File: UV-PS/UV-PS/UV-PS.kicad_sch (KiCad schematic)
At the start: 15 parts, among them J1 Conn_01x02_Female, J2 Conn_01x02_Female, U1 MC33063AP

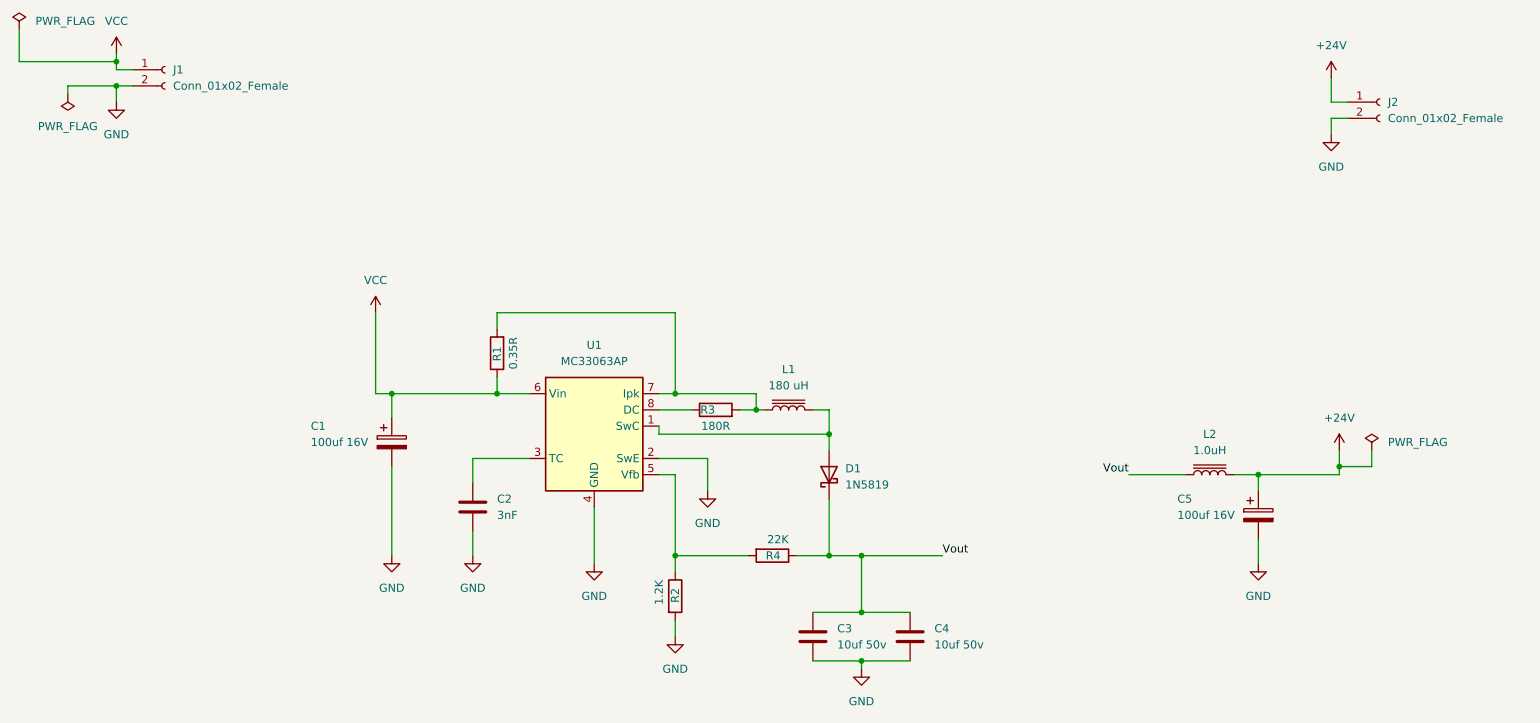
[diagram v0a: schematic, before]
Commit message: IC Change
Changed complete design.
From Mc33062 to LMR64010
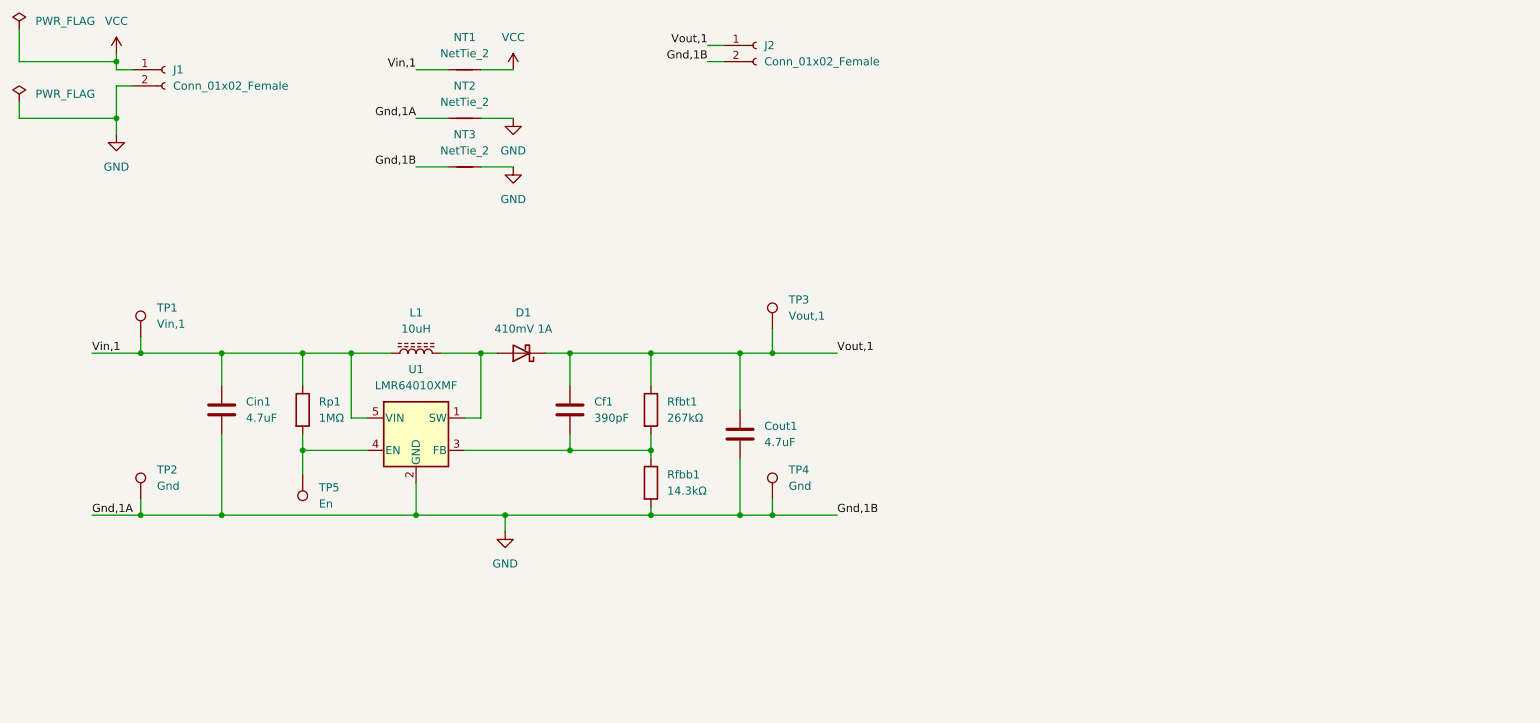
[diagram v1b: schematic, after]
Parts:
- removed C1, C5: 100uf 16V, Capacitor_THT:CP_Radial_D6.3mm_P2.50mm, symbol Device:C_Polarized
- removed C2: 3nF, Capacitor_SMD:C_0603_1608Metric_Pad1.08x0.95mm_HandSolder, symbol Device:C
- removed C3, C4: 10uf 50v, Capacitor_SMD:C_1206_3216Metric_Pad1.33x1.80mm_HandSolder, symbol Device:C
- removed D1: 1N5819, Diode_THT:D_DO-41_SOD81_P10.16mm_Horizontal, symbol Diode:1N5819
- removed L1: 180 uH, Custom Parts:7447669218, symbol Device:L_Iron
- removed L2: 1.0uH, Resistor_THT:R_Axial_DIN0207_L6.3mm_D2.5mm_P7.62mm_Horizontal, symbol Device:L_Iron
- removed R1: 0.35R, Resistor_SMD:R_2512_6332Metric_Pad1.40x3.35mm_HandSolder, symbol Device:R
- removed R2: 1.2K, Resistor_THT:R_Axial_DIN0207_L6.3mm_D2.5mm_P7.62mm_Horizontal, symbol Device:R
- removed R3: 180R, Resistor_SMD:R_1206_3216Metric_Pad1.30x1.75mm_HandSolder, symbol Device:R
- removed R4: 22K, Resistor_THT:R_Axial_DIN0207_L6.3mm_D2.5mm_P7.62mm_Horizontal, symbol Device:R
- removed U1: MC33063AP, Package_DIP:DIP-8_W7.62mm, symbol Regulator_Switching:MC33063AP
- added Cf1: 390pF, Capacitor_SMD:C_0805_2012Metric_Pad1.18x1.45mm_HandSolder, symbol Device:C
- added Cin1, Cout1: 4.7uF, Capacitor_SMD:C_1206_3216Metric_Pad1.33x1.80mm_HandSolder, symbol Device:C
- added D1: 410mV 1A, Diode_SMD:D_SMA, symbol Diode:B130-E3
- added L1: 10uH, Custom Parts:SDR0403-100ML, symbol Device:L_Ferrite
- added NT1: NetTie_2, symbol Device:NetTie_2
- added NT2, NT3: NetTie_2, NetTie:NetTie-2_SMD_Pad2.0mm, symbol Device:NetTie_2
- added Rfbb1: 14.3kΩ, Resistor_SMD:R_1206_3216Metric_Pad1.30x1.75mm_HandSolder, symbol Device:R
- added Rfbt1: 267kΩ, Resistor_SMD:R_1206_3216Metric_Pad1.30x1.75mm_HandSolder, symbol Device:R
- added Rp1: 1MΩ, Resistor_SMD:R_1206_3216Metric_Pad1.30x1.75mm_HandSolder, symbol Device:R
- added TP1: Vin,1, symbol Connector:TestPoint
- added TP2, TP4: Gnd, TestPoint:TestPoint_Keystone_5000-5004_Miniature, symbol Connector:TestPoint
- added TP3: Vout,1, TestPoint:TestPoint_Keystone_5000-5004_Miniature, symbol Connector:TestPoint
- added TP5: En, TestPoint:TestPoint_Keystone_5000-5004_Miniature, symbol Connector:TestPoint
- added U1: LMR64010XMF, Package_TO_SOT_SMD:SOT-23-5, symbol Regulator_Switching:LMR64010XMF
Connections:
- net GND: now also Cin1.2, Cout1.2, NT2.1, NT2.2, NT3.1, NT3.2, Rfbb1.2, TP2.1, TP4.1, U1.2 (GND)
- net VCC: now also NT1.2
- net +24V renamed Vout,1
- net Vout,1: now also Cf1.1, Cout1.1, D1.1 (K), Rfbt1.1, TP3.1
- new net: Cf1.2, Rfbb1.1, Rfbt1.2, U1.3 (FB)
- new net: D1.2 (A), L1.2, U1.1 (SW)
- new net: Rp1.2, TP5.1, U1.4 (EN)
- new net Vin,1: Cin1.1, L1.1, NT1.1, Rp1.1, TP1.1, U1.5 (VIN)
